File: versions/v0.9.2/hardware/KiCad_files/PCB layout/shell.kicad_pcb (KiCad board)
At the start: 2 copper layers, 30.5 x 52.1 mm, 2 parts, among them P6 CONN_01X12, P7 arduino_half_moonX24

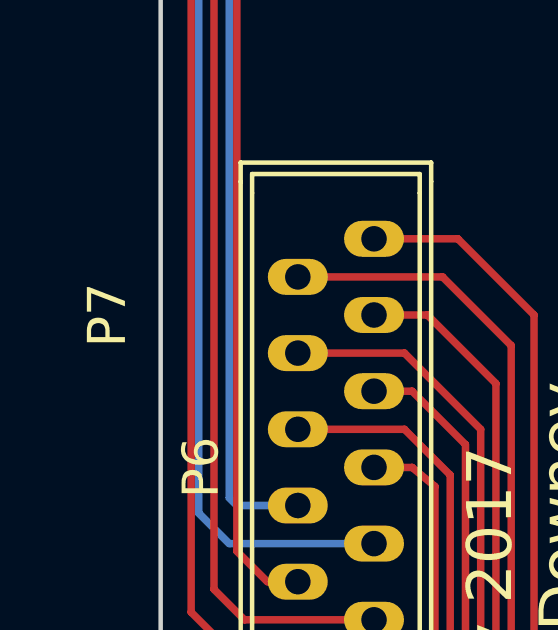
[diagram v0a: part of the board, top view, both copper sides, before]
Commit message: Modernize v0.9.2 KiCad files for KiCad 9
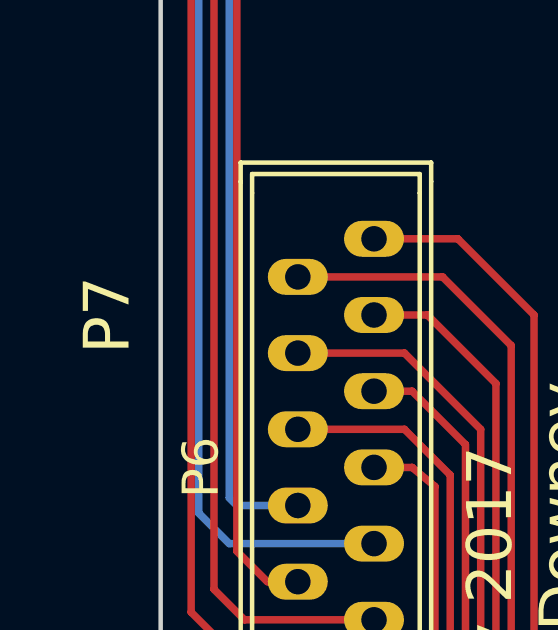
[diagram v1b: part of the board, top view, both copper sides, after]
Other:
- net class Default removed
